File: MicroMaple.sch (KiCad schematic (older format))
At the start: 44 parts, among them P1 USB_OTG, P2 CONN_01X14, P3 CONN_01X14, P4 CONN_01X12, P5 CONN_01X01, P6 CONN_01X01, P7 CONN_01X01, P8 CONN_01X01, Q1 8050, Q2 8050, SW1 USR_BUT, SW2 RST_BUTTON, U1 STM32F103C8T6, U2 XC6206P332MR, U3 XC6206P332MR, X1 8MHz_OSC

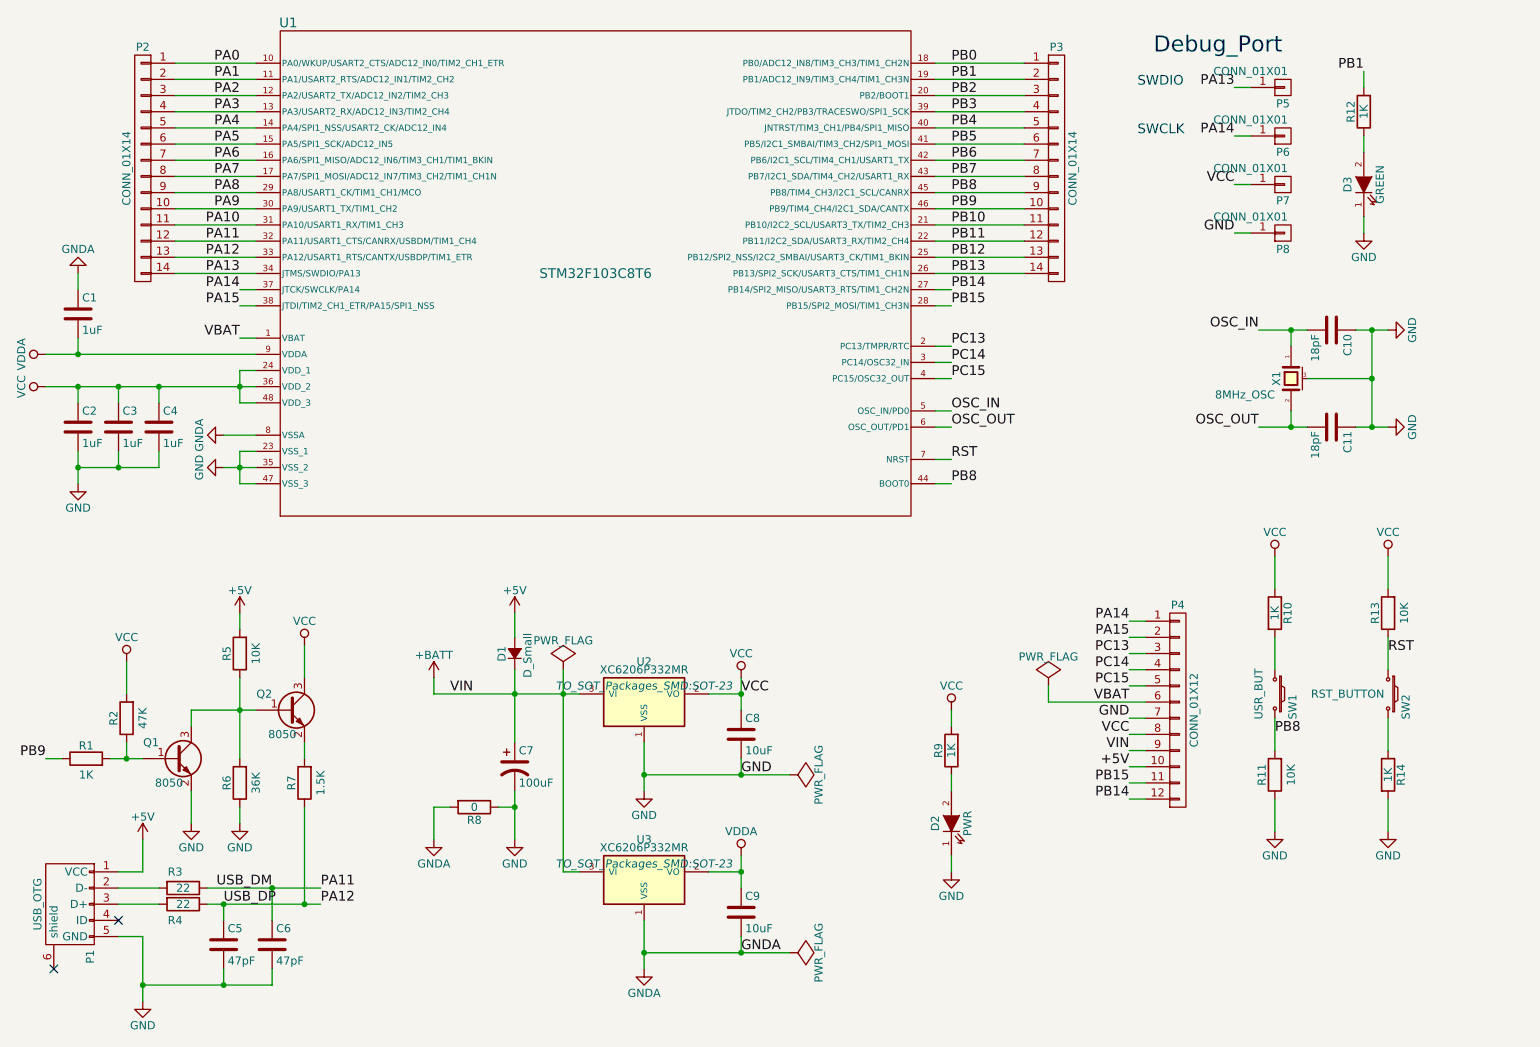
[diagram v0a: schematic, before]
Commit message: 1.remove the USB disconnect circuit. 2.export v1.1 pdf. 3.add smslit logo lib
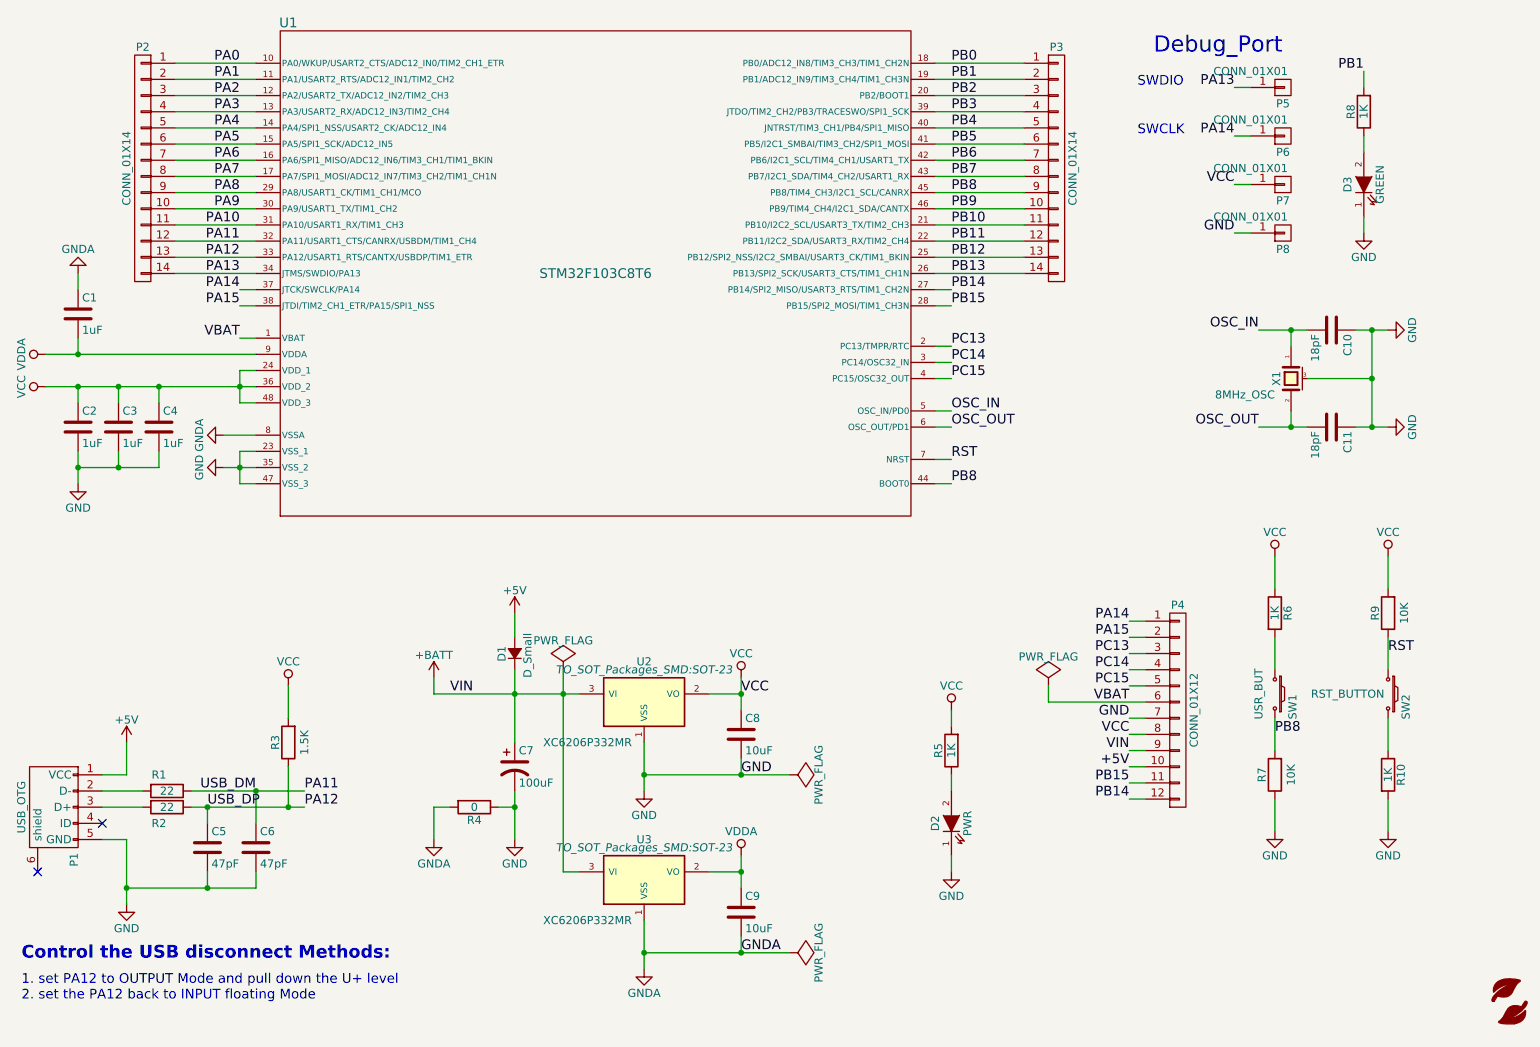
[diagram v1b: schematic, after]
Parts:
- removed Q1, Q2: 8050, TO_SOT_Packages_SMD:SOT-23, symbol Q_NPN_BEC
- removed R1: 1K, Resistors_SMD:R_0603, symbol R
- removed R2: 47K, Resistors_SMD:R_0603, symbol R
- removed R5: 10K, Resistors_SMD:R_0603, symbol R
- removed R6: 36K, Resistors_SMD:R_0603, symbol R
- renumbered R3 to R1, R14 to R10, R4 to R2, R7 to R3, R8 to R4, R9 to R5, R10 to R6, R11 to R7, R12 to R8, R13 to R9
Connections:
- net VCC: now also R3.2
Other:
- note added: "1. set PA12 to OUTPUT Mode and pull down the U+ level\n2. set the PA12 back to INPUT floating Mode"
- note added: "Control the USB disconnect Methods:"
- moved on the sheet: C5, C6, P1, R1, R2, R3

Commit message: Micro Maple Version1.1 : 1. update the sch and netlist file; 2. finish pcb trace layout
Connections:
- net PB0: now also R8.2
- net PB1: no longer R8.2
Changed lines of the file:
@@
 $EndComp
 Text Label 9950 1100 2    60   ~ 0
-PB1
+PB0
 $Comp
 L R R5
@@
 1. set PA12 to OUTPUT Mode and pull down the U+ level\n2. set the PA12 back to INPUT floating Mode
 $Comp
-L LOGO #G?
+L LOGO #G1
 U 1 1 5805F4C9
 P 10850 6850
-F 0 "#G?" H 10850 6693 60  0001 C CNN
+F 0 "#G1" H 10850 6693 60  0001 C CNN
 F 1 "LOGO" H 10850 7007 60  0001 C CNN
 F 2 "" H 10850 6850 60  0001 C CNN

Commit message: because the mistake in m2OLED pcb design, change the position of GND\VCC\VBAT
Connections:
- net GND: now also P4.6 (P6); no longer P4.7 (P7)
- net VBAT: now also P4.8 (P8); no longer P4.6 (P6)
- net VCC: now also P4.7 (P7); no longer P4.8 (P8)
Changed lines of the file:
@@
 Text Label 8500 4900 2    60   ~ 0
 PC15
+Text Label 8500 5200 2    60   ~ 0
+VBAT
 Text Label 8500 5000 2    60   ~ 0
-VBAT
+GND
 Text Label 8500 5100 2    60   ~ 0
-GND
-Text Label 8500 5200 2    60   ~ 0
 VCC
 Text Label 8500 5300 2    60   ~ 0
@@
 	8600 4900 8500 4900
 Wire Wire Line
-	8000 5000 8600 5000
-Wire Wire Line
-	8600 5100 8500 5100
-Wire Wire Line
-	8600 5200 8500 5200
-Wire Wire Line
 	8600 5300 8500 5300
 Wire Wire Line
@@
 $EndComp
 Wire Wire Line
-	8000 4900 8000 5000
+	8000 4900 8000 5200
 Text Label 6100 5450 0    60   ~ 0
 GND
@@
 	1    0    0    -1
 $EndComp
+Wire Wire Line
+	8600 5000 8500 5000
+Wire Wire Line
+	8600 5100 8500 5100
+Wire Wire Line
+	8000 5200 8600 5200
 $EndSCHEMATC
